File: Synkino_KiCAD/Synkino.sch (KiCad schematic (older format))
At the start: 45 parts

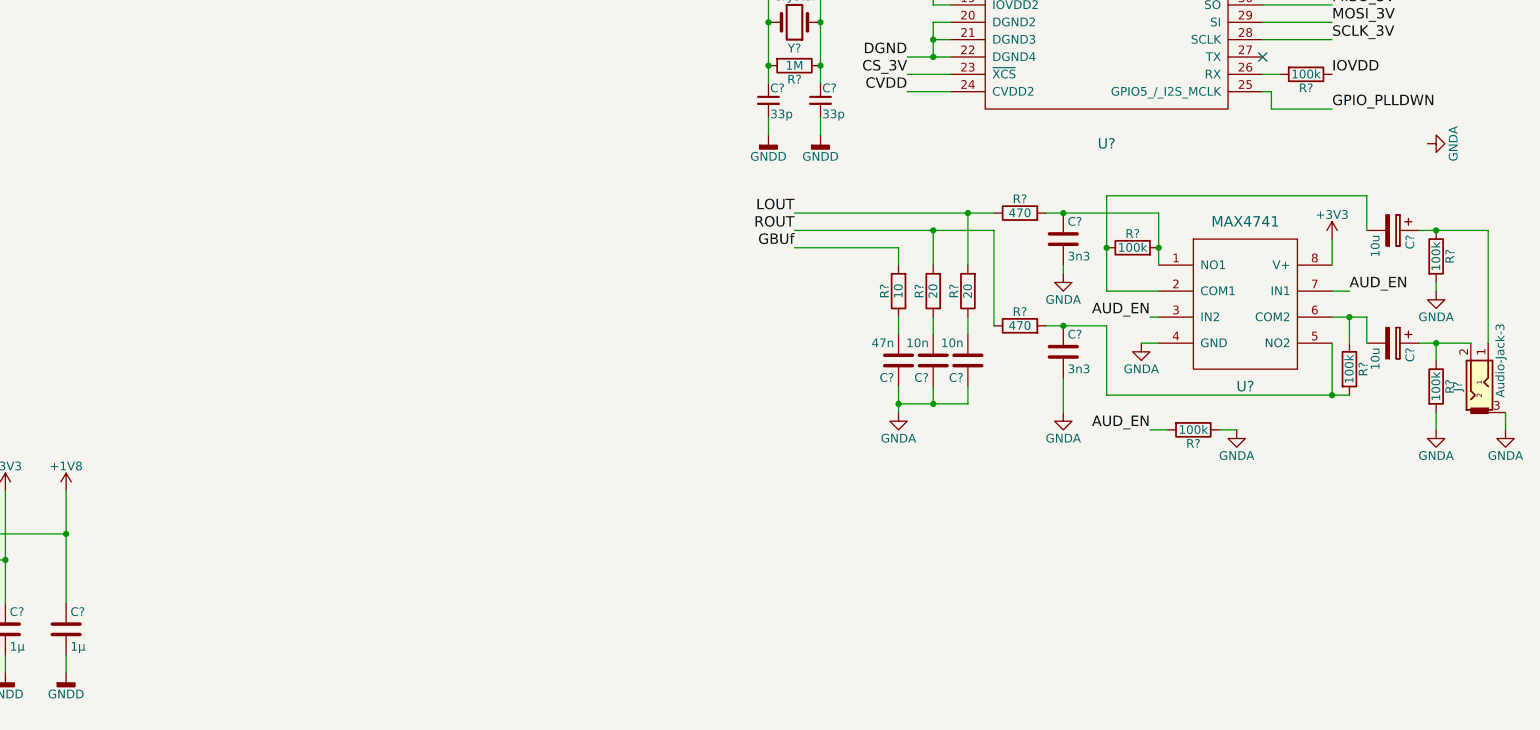
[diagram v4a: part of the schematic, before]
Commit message: Add power decoupling caps
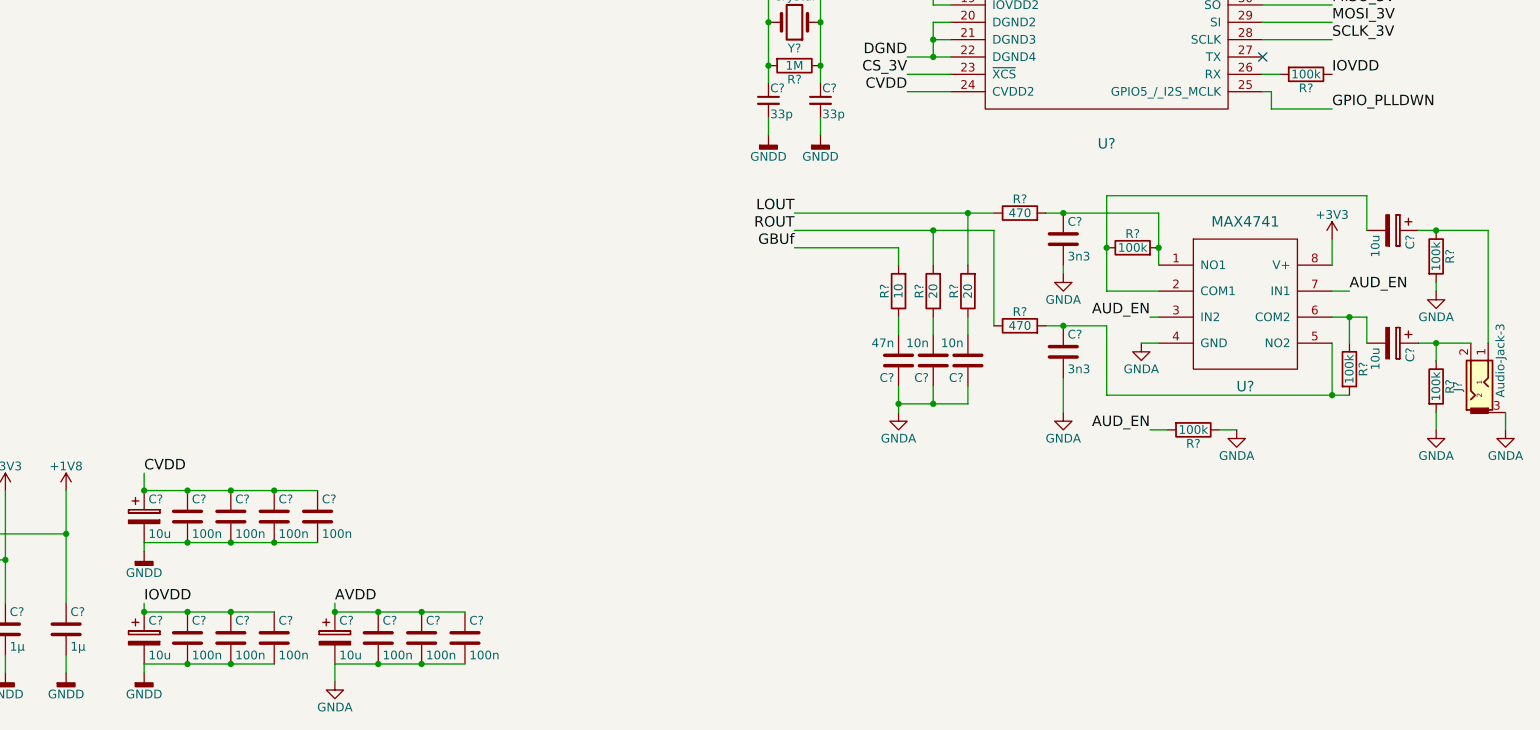
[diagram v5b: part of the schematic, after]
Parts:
- added C? (x10): 100n, symbol C
- added C? (x3): 10u, symbol CP
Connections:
- net +1V8: now also C?.1, C?.1, C?.1, C?.1, C?.1
- net +3V3: now also C?.1, C?.1, C?.1, C?.1
- net GNDA: now also C?.2, C?.2, C?.2, C?.2
- net GNDD: now also C?.2, C?.2, C?.2, C?.2, C?.2, C?.2, C?.2, C?.2, C?.2
- net VDDA: now also C?.1, C?.1, C?.1, C?.1
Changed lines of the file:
@@
 Connection ~ 10450 4950
-$Comp
-L GNDA #PWR031
-U 1 1 5A9AE454
-P 10400 4450
-F 0 "#PWR031" H 10400 4200 50  0001 C CNN
-F 1 "GNDA" H 10400 4300 50  0000 C CNN
-F 2 "" H 10400 4450 50  0001 C CNN
-F 3 "" H 10400 4450 50  0001 C CNN
-	1    10400 4450
-	0    -1   -1   0
-$EndComp
 $Comp
 L MAX4741 U?
@@
 	10450 5600 10450 5700
 Connection ~ 10450 5600
+$Comp
+L C C?
+U 1 1 5A9B4366
+P 3250 6600
+F 0 "C?" H 3275 6700 50  0000 L CNN
+F 1 "100n" H 3275 6500 50  0000 L CNN
+F 2 "" H 3288 6450 50  0001 C CNN
+F 3 "" H 3250 6600 50  0001 C CNN
+	1    3250 6600
+	1    0    0    -1
+$EndComp
+$Comp
+L C C?
+U 1 1 5A9B4475
+P 3500 6600
+F 0 "C?" H 3525 6700 50  0000 L CNN
+F 1 "100n" H 3525 6500 50  0000 L CNN
+F 2 "" H 3538 6450 50  0001 C CNN
+F 3 "" H 3500 6600 50  0001 C CNN
+	1    3500 6600
+	1    0    0    -1
+$EndComp
+$Comp
+L C C?
+U 1 1 5A9B4516
+P 3750 6600
+F 0 "C?" H 3775 6700 50  0000 L CNN
+F 1 "100n" H 3775 6500 50  0000 L CNN
+F 2 "" H 3788 6450 50  0001 C CNN
+F 3 "" H 3750 6600 50  0001 C CNN
+	1    3750 6600
+	1    0    0    -1
+$EndComp
+$Comp
+L C C?
+U 1 1 5A9B45B7
+P 4000 6600
+F 0 "C?" H 4025 6700 50  0000 L CNN
+F 1 "100n" H 4025 6500 50  0000 L CNN
+F 2 "" H 4038 6450 50  0001 C CNN
+F 3 "" H 4000 6600 50  0001 C CNN
+	1    4000 6600
+	1    0    0    -1
+$EndComp
+$Comp
+L CP C?
+U 1 1 5A9B4831
+P 3000 6600
+F 0 "C?" H 3025 6700 50  0000 L CNN
+F 1 "10u" H 3025 6500 50  0000 L CNN
+F 2 "" H 3038 6450 50  0001 C CNN
+F 3 "" H 3000 6600 50  0001 C CNN
+	1    3000 6600
+	1    0    0    -1
+$EndComp
+$Comp
+L GNDD #PWR?
+U 1 1 5A9B4958
+P 3000 6800
+F 0 "#PWR?" H 3000 6550 50  0001 C CNN
+F 1 "GNDD" H 3000 6675 50  0000 C CNN
+F 2 "" H 3000 6800 50  0001 C CNN
+F 3 "" H 3000 6800 50  0001 C CNN
+	1    3000 6800
+	1    0    0    -1
+$EndComp
+Wire Wire Line
+	3000 6800 3000 6750
+Wire Wire Line
+	3000 6750 4000 6750
+Wire Wire Line
+	3000 6450 4000 6450
+Connection ~ 3250 6450
+Connection ~ 3500 6450
+Connection ~ 3750 6450
+Connection ~ 3750 6750
+Connection ~ 3500 6750
+Connection ~ 3250 6750
+$Comp
+L C C?
+U 1 1 5A9B4DB1
+P 3250 7300
+F 0 "C?" H 3275 7400 50  0000 L CNN
+F 1 "100n" H 3275 7200 50  0000 L CNN
+F 2 "" H 3288 7150 50  0001 C CNN
+F 3 "" H 3250 7300 50  0001 C CNN
+	1    3250 7300
+	1    0    0    -1
+$EndComp
+$Comp
+L C C?
+U 1 1 5A9B4DB7
+P 3500 7300
+F 0 "C?" H 3525 7400 50  0000 L CNN
+F 1 "100n" H 3525 7200 50  0000 L CNN
+F 2 "" H 3538 7150 50  0001 C CNN
+F 3 "" H 3500 7300 50  0001 C CNN
+	1    3500 7300
+	1    0    0    -1
+$EndComp
+$Comp
+L C C?
+U 1 1 5A9B4DBD
+P 3750 7300
+F 0 "C?" H 3775 7400 50  0000 L CNN
+F 1 "100n" H 3775 7200 50  0000 L CNN
+F 2 "" H 3788 7150 50  0001 C CNN
+F 3 "" H 3750 7300 50  0001 C CNN
+	1    3750 7300
+	1    0    0    -1
+$EndComp
+$Comp
+L CP C?
+U 1 1 5A9B4DC9
+P 3000 7300
+F 0 "C?" H 3025 7400 50  0000 L CNN
+F 1 "10u" H 3025 7200 50  0000 L CNN
+F 2 "" H 3038 7150 50  0001 C CNN
+F 3 "" H 3000 7300 50  0001 C CNN
+	1    3000 7300
+	1    0    0    -1
+$EndComp
+$Comp
+L GNDD #PWR?
+U 1 1 5A9B4DCF
+P 3000 7500
+F 0 "#PWR?" H 3000 7250 50  0001 C CNN
+F 1 "GNDD" H 3000 7375 50  0000 C CNN
+F 2 "" H 3000 7500 50  0001 C CNN
+F 3 "" H 3000 7500 50  0001 C CNN
+	1    3000 7500
+	1    0    0    -1
+$EndComp
+Wire Wire Line
+	3000 7500 3000 7450
+Connection ~ 3250 7150
+Connection ~ 3500 7150
+Connection ~ 3500 7450
+Connection ~ 3250 7450
+Wire Wire Line
+	3000 7150 3750 7150
+Wire Wire Line
+	3000 7450 3750 7450
+$Comp
+L C C?
+U 1 1 5A9B5358
+P 4350 7300
+F 0 "C?" H 4375 7400 50  0000 L CNN
+F 1 "100n" H 4375 7200 50  0000 L CNN
+F 2 "" H 4388 7150 50  0001 C CNN
+F 3 "" H 4350 7300 50  0001 C CNN
+	1    4350 7300
+	1    0    0    -1
+$EndComp
+$Comp
+L C C?
+U 1 1 5A9B535E
+P 4600 7300
+F 0 "C?" H 4625 7400 50  0000 L CNN
+F 1 "100n" H 4625 7200 50  0000 L CNN
+F 2 "" H 4638 7150 50  0001 C CNN
+F 3 "" H 4600 7300 50  0001 C CNN
+	1    4600 7300
+	1    0    0    -1
+$EndComp
+$Comp
+L C C?
+U 1 1 5A9B5364
+P 4850 7300
+F 0 "C?" H 4875 7400 50  0000 L CNN
+F 1 "100n" H 4875 7200 50  0000 L CNN
+F 2 "" H 4888 7150 50  0001 C CNN
+F 3 "" H 4850 7300 50  0001 C CNN
+	1    4850 7300
+	1    0    0    -1
+$EndComp
+$Comp
+L CP C?
+U 1 1 5A9B536A
+P 4100 7300
+F 0 "C?" H 4125 7400 50  0000 L CNN
+F 1 "10u" H 4125 7200 50  0000 L CNN
+F 2 "" H 4138 7150 50  0001 C CNN
+F 3 "" H 4100 7300 50  0001 C CNN
+	1    4100 7300
+	1    0    0    -1
+$EndComp
+Wire Wire Line
+	4100 7450 4100 7550
+Connection ~ 4350 7150
+Connection ~ 4600 7150
+Connection ~ 4600 7450
+Connection ~ 4350 7450
+Wire Wire Line
+	4100 7150 4850 7150
+Wire Wire Line
+	4100 7450 4850 7450
+$Comp
+L GNDA #PWR?
+U 1 1 5A9B55C3
+P 4100 7550
+F 0 "#PWR?" H 4100 7300 50  0001 C CNN
+F 1 "GNDA" H 4100 7400 50  0000 C CNN
+F 2 "" H 4100 7550 50  0001 C CNN
+F 3 "" H 4100 7550 50  0001 C CNN
+	1    4100 7550
+	1    0    0    -1
+$EndComp
+Text Label 3000 6350 0    60   ~ 0
+CVDD
+Wire Wire Line
+	3000 6350 3000 6450
+Connection ~ 3000 6450
+Text Label 3000 7100 0    60   ~ 0
+IOVDD
+Wire Wire Line
+	3000 7100 3000 7150
+Connection ~ 3000 7150
+Text Label 4100 7100 0    60   ~ 0
+AVDD
+Wire Wire Line
+	4100 7100 4100 7150
+Connection ~ 4100 7150
 $EndSCHEMATC

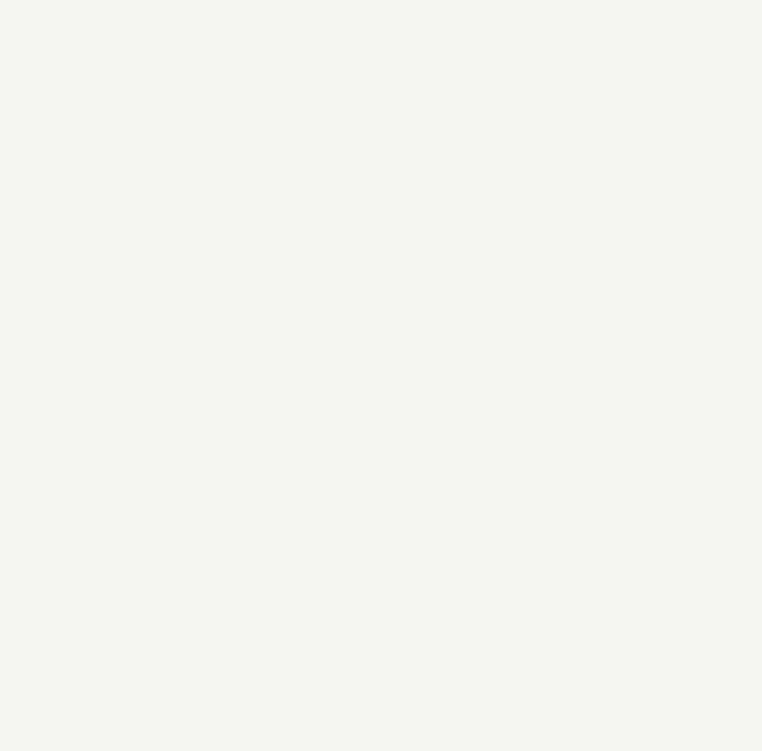
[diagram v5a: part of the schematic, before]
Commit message: Adding uSD Card
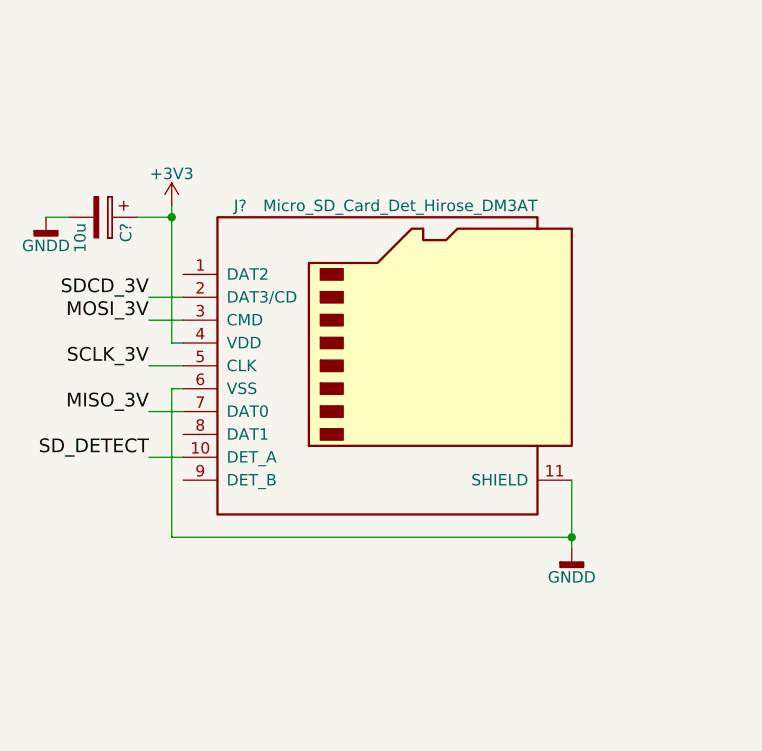
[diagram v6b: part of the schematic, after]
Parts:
- added C?: 10u, symbol CP
- added J?: Micro_SD_Card_Det_Hirose_DM3AT, symbol Micro_SD_Card_Det_Hirose_DM3AT
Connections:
- net +3V3: now also C?.1, J?.4 (VDD)
- net GNDD: now also C?.2, J?.11 (SHIELD), J?.6 (VSS)
- net MISO_3V: now also J?.7 (DAT0)
- net MOSI_3V: now also J?.3 (CMD)
- net SCLK_3V: now also J?.5 (CLK)
- new net SDCD_3V: J?.2 (DAT3/CD)
- new net SD_DETECT: J?.10 (DET_A)
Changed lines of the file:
@@
 	4100 7100 4100 7150
 Connection ~ 4100 7150
+$Comp
+L Micro_SD_Card_Det_Hirose_DM3AT J?
+U 1 1 5A9BABF0
+P 2250 4100
+F 0 "J?" H 1600 4800 50  0000 C CNN
+F 1 "Micro_SD_Card_Det_Hirose_DM3AT" H 2900 4800 50  0000 R CNN
+F 2 "" H 4300 4800 50  0001 C CNN
+F 3 "" H 2250 4200 50  0001 C CNN
+	1    2250 4100
+	1    0    0    -1
+$EndComp
+Text Label 1200 4300 2    60   ~ 0
+MISO_3V
+Text Label 1200 3900 2    60   ~ 0
+MOSI_3V
+Text Label 1200 4100 2    60   ~ 0
+SCLK_3V
+Text Label 1200 3800 2    60   ~ 0
+SDCD_3V
+Wire Wire Line
+	1350 4200 1300 4200
+Wire Wire Line
+	1300 4200 1300 4850
+Wire Wire Line
+	1300 4850 3050 4850
+Wire Wire Line
+	3050 4600 3050 4900
+$Comp
+L GNDD #PWR?
+U 1 1 5A9BCC04
+P 3050 4900
+F 0 "#PWR?" H 3050 4650 50  0001 C CNN
+F 1 "GNDD" H 3050 4775 50  0000 C CNN
+F 2 "" H 3050 4900 50  0001 C CNN
+F 3 "" H 3050 4900 50  0001 C CNN
+	1    3050 4900
+	1    0    0    -1
+$EndComp
+Connection ~ 3050 4850
+$Comp
+L +3V3 #PWR?
+U 1 1 5A9BCFB7
+P 1300 3400
+F 0 "#PWR?" H 1300 3250 50  0001 C CNN
+F 1 "+3V3" H 1300 3540 50  0000 C CNN
+F 2 "" H 1300 3400 50  0001 C CNN
+F 3 "" H 1300 3400 50  0001 C CNN
+	1    1300 3400
+	1    0    0    -1
+$EndComp
+Wire Wire Line
+	1300 3400 1300 4000
+Wire Wire Line
+	1300 4000 1350 4000
+$Comp
+L CP C?
+U 1 1 5A9BD1CD
+P 1000 3450
+F 0 "C?" H 1025 3550 50  0000 L CNN
+F 1 "10u" H 1025 3350 50  0000 L CNN
+F 2 "" H 1038 3300 50  0001 C CNN
+F 3 "" H 1000 3450 50  0001 C CNN
+	1    1000 3450
+	0    1    1    0
+$EndComp
+Wire Wire Line
+	1150 3450 1300 3450
+Connection ~ 1300 3450
+$Comp
+L GNDD #PWR?
+U 1 1 5A9BD4F9
+P 750 3450
+F 0 "#PWR?" H 750 3200 50  0001 C CNN
+F 1 "GNDD" H 750 3325 50  0000 C CNN
+F 2 "" H 750 3450 50  0001 C CNN
+F 3 "" H 750 3450 50  0001 C CNN
+	1    750  3450
+	1    0    0    -1
+$EndComp
+Wire Wire Line
+	750  3450 850  3450
+Wire Wire Line
+	1200 3900 1350 3900
+Wire Wire Line
+	1200 3800 1350 3800
+Wire Wire Line
+	1200 4100 1350 4100
+Wire Wire Line
+	1200 4300 1350 4300
+Text Label 1200 4500 2    60   ~ 0
+SD_DETECT
+Wire Wire Line
+	1200 4500 1350 4500
 $EndSCHEMATC

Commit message: Schematics Progress
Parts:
- added R? (x4): 100k, symbol R
- added U?: 74HC4050, symbol 74HC4050
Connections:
- net +3V3: now also R?.2, R?.2, R?.2, U?.1 (VCC)
- net CS_3V: now also U?.10 (4Y)
- net GNDD: now also R?.2, U?.8 (GND)
- net MOSI_3V: now also U?.4 (2Y)
- net RST_3V: now also U?.2 (1Y)
- net SCLK_3V: now also U?.6 (3Y)
- net XDCS_3V: now also U?.15 (6Y)
- net SD_DETECT: no longer names the net of J?.10 (DET_A)
- new net CS_5V: R?.1, U?.9 (4A)
- new net MOSI_5V: U?.5 (2A)
- new net RST_5V: R?.1, U?.3 (1A)
- new net SCLK_5V: U?.7 (3A)
- new net SDCS_3V: U?.12 (5Y)
- new net SDCS_5V: R?.1, U?.11 (5A)
- new net XDCS_5V: R?.1, U?.14 (6A)
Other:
- moved on the sheet: C?, D?, J?, Q?, R?, U?, U?A, U?B, U?C, Y?
